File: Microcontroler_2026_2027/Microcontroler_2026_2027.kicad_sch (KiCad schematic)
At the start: 0 parts

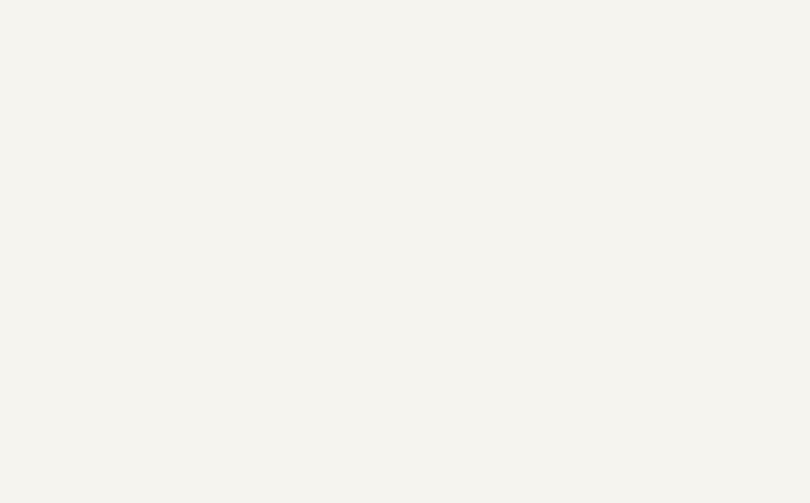
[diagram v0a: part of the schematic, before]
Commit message: Added telemetry station schematic and wired SPI to the main controller
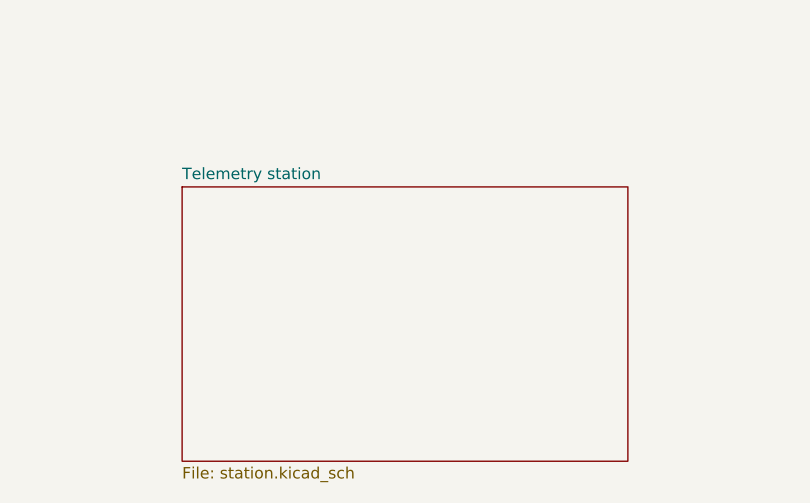
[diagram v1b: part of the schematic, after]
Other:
- added sheet Telemetry station (station.kicad_sch)
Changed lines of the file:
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@@
+	)
+	(sheet
+		(at 212.09 87.63)
+		(size 49.53 30.48)
+		(exclude_from_sim no)
+		(in_bom yes)
+		(on_board yes)
+		(dnp no)
+		(fields_autoplaced yes)
+		(stroke
+			(width 0.1524)
+			(type solid)
+		)
+		(fill
+			(color 0 0 0 0)
+		)
+		(property "Sheetname" "Telemetry station"
+			(at 212.09 86.9184 0)
+			(show_name no)
+			(do_not_autoplace no)
+			(effects
+				(font
+					(size 1.27 1.27)
+				)
+				(justify left bottom)
+			)
+		)
+		(property "Sheetfile" "station.kicad_sch"
+			(at 212.09 118.6946 0)
+			(show_name no)
+			(do_not_autoplace no)
+			(effects
+				(font
+					(size 1.27 1.27)
+				)
+				(justify left top)
+			)
+		)
+		(instances
+			(project "Microcontroler_2026_2027"
+				(path "/e4471f3f-0501-483d-9258-b42d5b5a0388"
+					(page "6")
+				)
+			)
+		)
 	)
 	(sheet
